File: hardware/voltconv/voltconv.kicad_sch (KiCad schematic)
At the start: 5 parts, among them Q1 2N7000, SW1 SW1

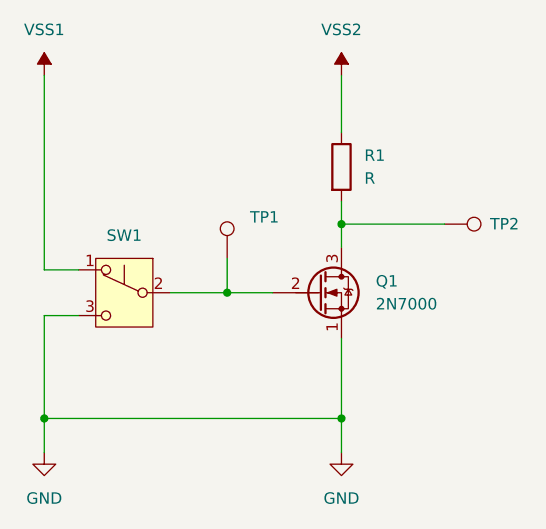
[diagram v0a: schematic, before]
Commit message: Changed VSS to VDD and stored results of measurements.
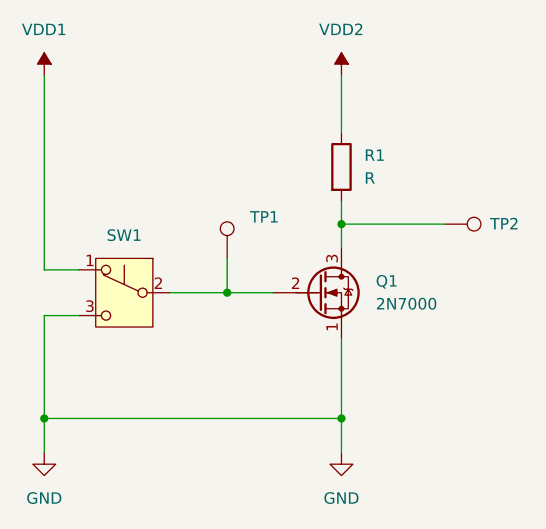
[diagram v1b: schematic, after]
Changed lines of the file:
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@@
       (effects (font (size 1.27 1.27)) hide)
     )
-    (property "Value" "VSS1" (at 86.36 69.85 0)
+    (property "Value" "VDD1" (at 86.36 69.85 0)
       (effects (font (size 1.27 1.27)))
     )
@@
       (effects (font (size 1.27 1.27)) hide)
     )
-    (property "Value" "VSS2" (at 119.38 69.85 0)
+    (property "Value" "VDD2" (at 119.38 69.85 0)
       (effects (font (size 1.27 1.27)))
     )
